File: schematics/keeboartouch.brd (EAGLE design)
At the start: 157.5 x 101.6 mm, 56 parts, among them K1 TOUCHKEY, K10 TOUCHKEY, K11 TOUCHKEY, K12 TOUCHKEY, K13 TOUCHKEY, K14 TOUCHKEY, K15 TOUCHKEY, K16 TOUCHKEY, K17 TOUCHKEY, K18 TOUCHKEY, K19 TOUCHKEY, K2 TOUCHKEY, K20 TOUCHKEY, K21 TOUCHKEY, K22 TOUCHKEY, K23 TOUCHKEY, K24 TOUCHKEY, K25 TOUCHKEY, K26 TOUCHKEY, K27 TOUCHKEY, K28 TOUCHKEY, K29 TOUCHKEY, K3 TOUCHKEY, K30 TOUCHKEY, K31 TOUCHKEY, K32 TOUCHKEY, K33 TOUCHKEY, K34 TOUCHKEY, K35 TOUCHKEY, K36 TOUCHKEY, K37 TOUCHKEY, K38 TOUCHKEY, K39 TOUCHKEY, K4 TOUCHKEY, K40 TOUCHKEY, K5 TOUCHKEY, K6 TOUCHKEY, K7 TOUCHKEY, K8 TOUCHKEY, K9 TOUCHKEY, U2 PRO_MICROSMD

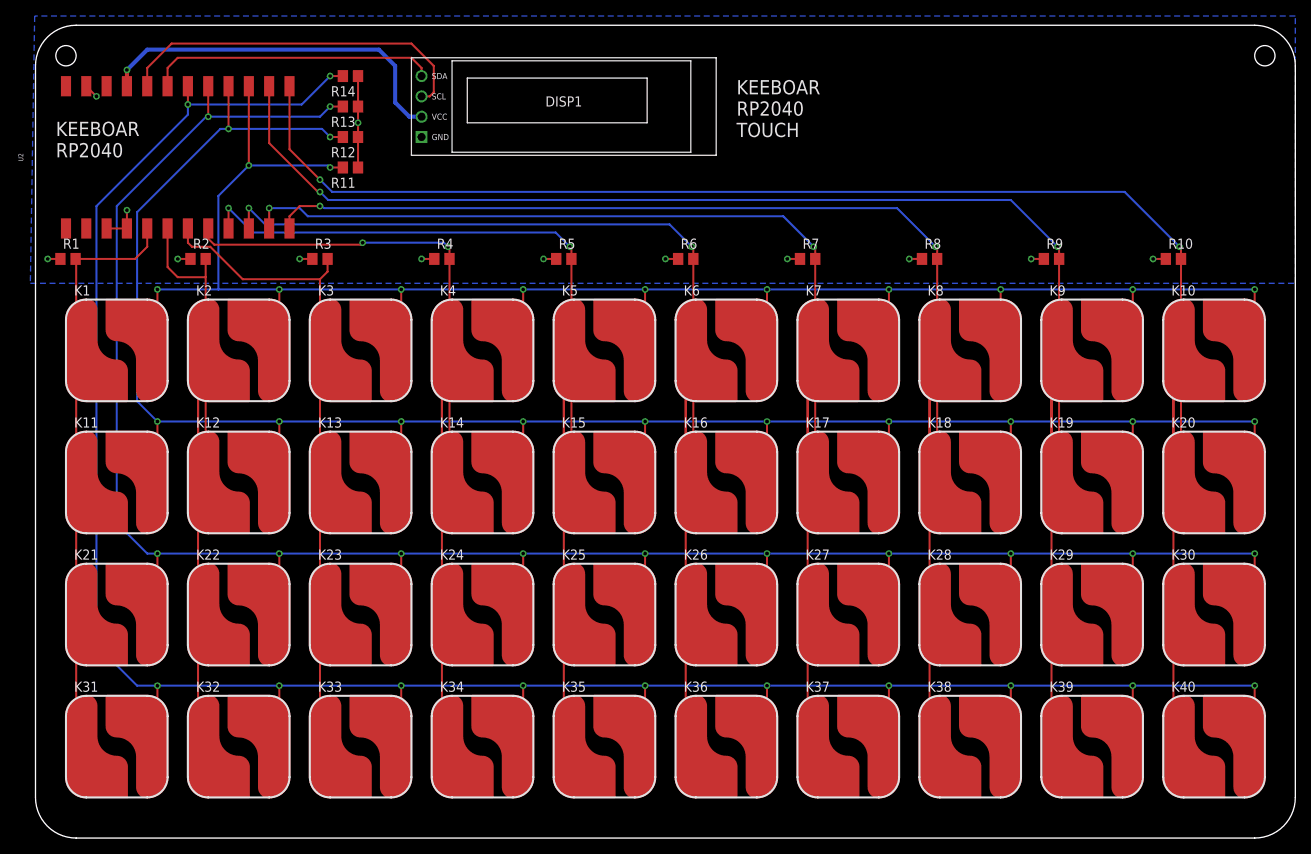
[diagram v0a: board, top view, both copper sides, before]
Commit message: four mount holes thx to jp
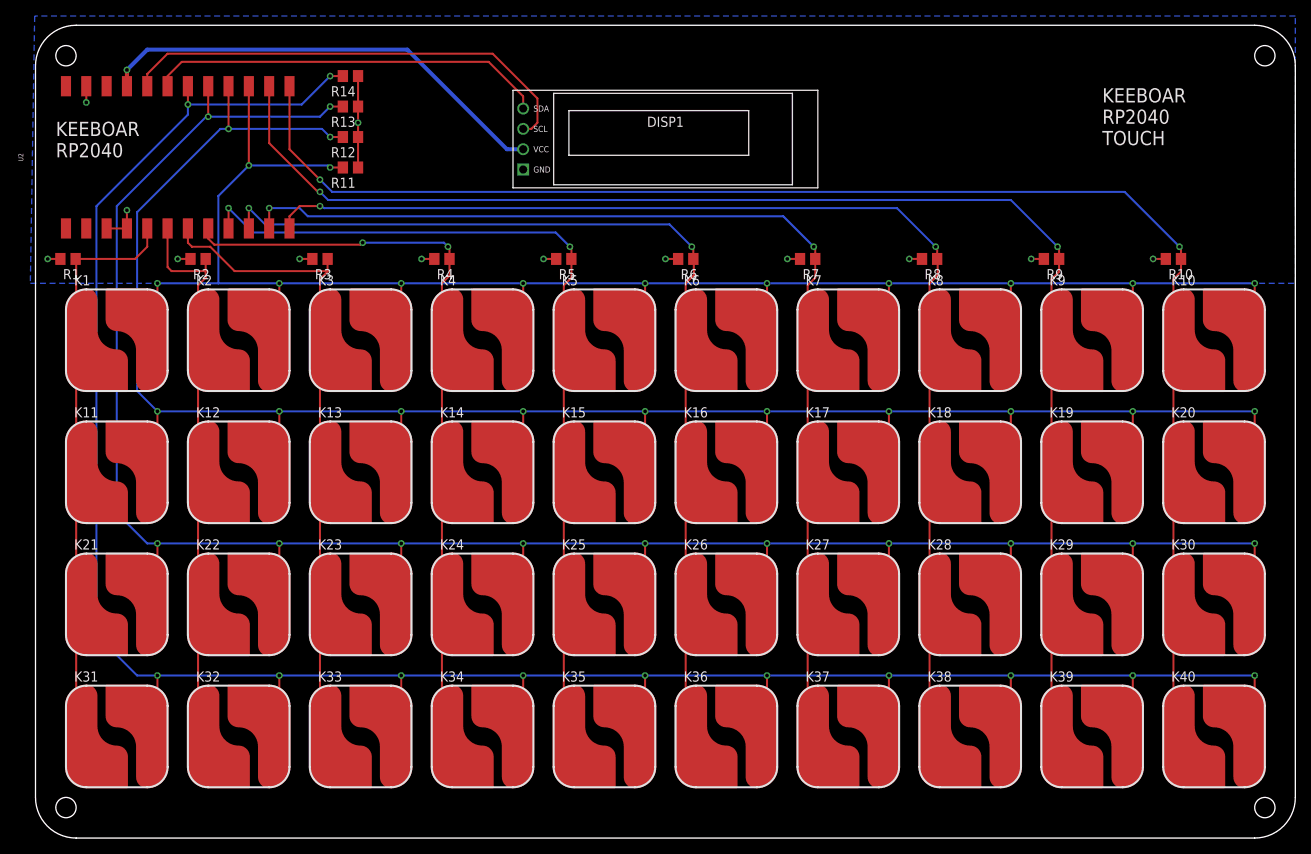
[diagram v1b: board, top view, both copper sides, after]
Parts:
- R1, R10, R11, R12, R13, R14, R2, R3, R4, R5, R6, R7, R8, R9: value (none) -> 1M
- moved DISP1 13.3 mm to (78.7, 87.4)
- moved K21 1.27 mm to (10.2, 29.2)
- moved K22 1.27 mm to (25.4, 29.2)
- moved K23 1.27 mm to (40.6, 29.2)
- moved K24 1.27 mm to (55.9, 29.2)
- moved K25 1.27 mm to (71.1, 29.2)
- moved K26 1.27 mm to (86.4, 29.2)
- moved K27 1.27 mm to (101.6, 29.2)
- moved K28 1.27 mm to (116.8, 29.2)
- moved K29 1.27 mm to (132.1, 29.2)
- moved K30 1.27 mm to (147.3, 29.2)
- moved K31 1.27 mm to (10.2, 12.7)
- moved K32 1.27 mm to (25.4, 12.7)
- moved K33 1.27 mm to (40.6, 12.7)
- moved K34 1.27 mm to (55.9, 12.7)
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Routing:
- net COL2: track 101.9 -> 75.0 mm
- net COL7: track 166.0 -> 139.4 mm
- net COL9: track 204.5 -> 177.8 mm
- net COL5: track 140.6 -> 114.0 mm
- net COL4: track 125.3 -> 98.6 mm
- net COL10: track 217.6 -> 190.9 mm
- net COL8: track 178.4 -> 151.7 mm
- net COL6: track 153.3 -> 126.7 mm
- net SDA: track 36.1 -> 49.8 mm
- net SCL: track 45.6 -> 58.8 mm
- net +3V3: track 46.1 -> 57.8 mm
- net ROW1: track 201.9 -> 195.6 mm
- net ROW3: track 246.1 -> 244.8 mm
- net COL1: track 77.9 -> 76.7 mm
- net ROW4: track 267.7 -> 266.4 mm
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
